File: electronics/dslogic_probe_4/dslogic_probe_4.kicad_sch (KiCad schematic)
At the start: 16 parts, among them J1 Conn_02x04_Odd_Even, J2 Conn_02x04_Odd_Even

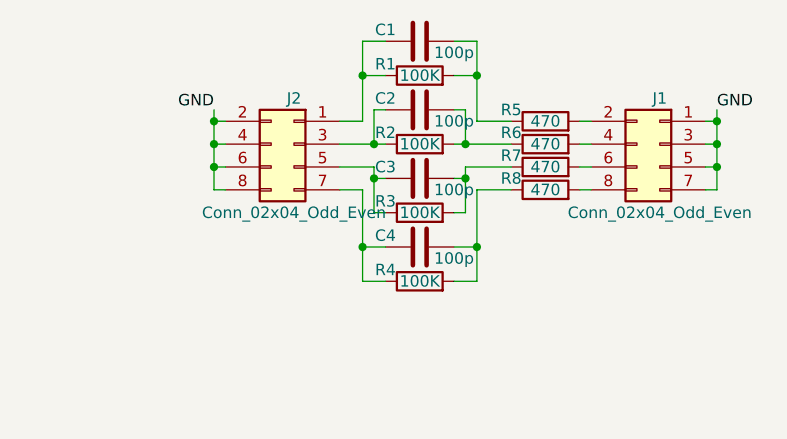
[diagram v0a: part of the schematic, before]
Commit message: edge footprints for probes
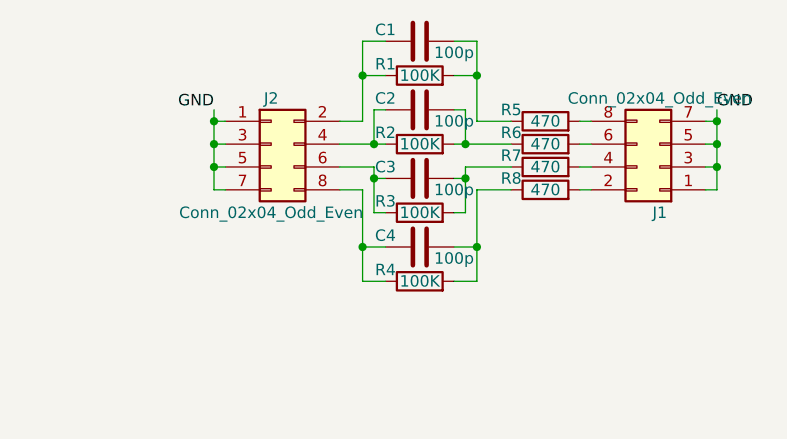
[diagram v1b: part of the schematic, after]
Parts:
- J1, J2: footprint Connector_PinSocket_1.27mm:PinSocket_2x04_P1.27mm_Vertical -> SquantorConnectors:Header-0127-2X04-EDGE
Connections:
- net GND: now also J2.1 (Pin_1), J2.3 (Pin_3), J2.5 (Pin_5), J2.7 (Pin_7); no longer J2.2 (Pin_2), J2.4 (Pin_4), J2.6 (Pin_6), J2.8 (Pin_8)
- net at C3.1, R3.1: now also J2.6 (Pin_6); no longer J2.5 (Pin_5)
- net at C1.1, R1.1: now also J2.2 (Pin_2); no longer J2.1 (Pin_1)
- net at C2.1, R2.1: now also J2.4 (Pin_4); no longer J2.3 (Pin_3)
- net at C4.1, R4.1: now also J2.8 (Pin_8); no longer J2.7 (Pin_7)
- net at R6.2: now also J1.6 (Pin_6); no longer J1.4 (Pin_4)
- net at J1.2 (Pin_2): now also R8.2; no longer R5.2
- net at R7.2: now also J1.4 (Pin_4); no longer J1.6 (Pin_6)
- net at J1.8 (Pin_8): now also R5.2; no longer R8.2
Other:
- moved on the sheet: J1
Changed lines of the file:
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@@
     (pin "2")
   )
-  (symbol (lib_id "Connector_Generic:Conn_02x04_Odd_Even") (at 73.66 38.1 0) (mirror y) (unit 1)
-    (in_bom yes) (on_board yes)
-    (property "Reference" "J2" (id 0) (at 73.66 33.02 0))
-    (property "Value" "Conn_02x04_Odd_Even" (id 1) (at 73.66 45.72 0))
-    (property "Footprint" "Connector_PinSocket_1.27mm:PinSocket_2x04_P1.27mm_Vertical" (id 2) (at 73.66 38.1 0)
-      (effects (font (size 1.27 1.27)) hide)
-    )
-    (property "Datasheet" "~" (id 3) (at 73.66 38.1 0)
+  (symbol (lib_id "Connector_Generic:Conn_02x04_Odd_Even") (at 71.12 38.1 0) (unit 1)
+    (in_bom yes) (on_board yes)
+    (property "Reference" "J2" (id 0) (at 71.12 33.02 0))
+    (property "Value" "Conn_02x04_Odd_Even" (id 1) (at 71.12 45.72 0))
+    (property "Footprint" "SquantorConnectors:Header-0127-2X04-EDGE" (id 2) (at 71.12 38.1 0)
+      (effects (font (size 1.27 1.27)) hide)
+    )
+    (property "Datasheet" "~" (id 3) (at 71.12 38.1 0)
       (effects (font (size 1.27 1.27)) hide)
     )
@@
     (pin "2")
   )
-  (symbol (lib_id "Connector_Generic:Conn_02x04_Odd_Even") (at 114.3 38.1 0) (mirror y) (unit 1)
-    (in_bom yes) (on_board yes)
-    (property "Reference" "J1" (id 0) (at 114.3 33.02 0))
-    (property "Value" "Conn_02x04_Odd_Even" (id 1) (at 114.3 45.72 0))
-    (property "Footprint" "Connector_PinSocket_1.27mm:PinSocket_2x04_P1.27mm_Vertical" (id 2) (at 114.3 38.1 0)
-      (effects (font (size 1.27 1.27)) hide)
-    )
-    (property "Datasheet" "~" (id 3) (at 114.3 38.1 0)
+  (symbol (lib_id "Connector_Generic:Conn_02x04_Odd_Even") (at 114.3 40.64 180) (unit 1)
+    (in_bom yes) (on_board yes)
+    (property "Reference" "J1" (id 0) (at 114.3 45.72 0))
+    (property "Value" "Conn_02x04_Odd_Even" (id 1) (at 114.3 33.02 0))
+    (property "Footprint" "SquantorConnectors:Header-0127-2X04-EDGE" (id 2) (at 114.3 40.64 0)
+      (effects (font (size 1.27 1.27)) hide)
+    )
+    (property "Datasheet" "~" (id 3) (at 114.3 40.64 0)
       (effects (font (size 1.27 1.27)) hide)
     )
@@
     )
     (path "/a72f7593-045b-4cee-9761-530bd4867197"
-      (reference "J1") (unit 1) (value "Conn_02x04_Odd_Even") (footprint "Connector_PinSocket_1.27mm:PinSocket_2x04_P1.27mm_Vertical")
+      (reference "J1") (unit 1) (value "Conn_02x04_Odd_Even") (footprint "SquantorConnectors:Header-0127-2X04-EDGE")
     )
     (path "/247d18a8-48ce-4e7f-9759-0eea4ad80e9a"
-      (reference "J2") (unit 1) (value "Conn_02x04_Odd_Even") (footprint "Connector_PinSocket_1.27mm:PinSocket_2x04_P1.27mm_Vertical")
+      (reference "J2") (unit 1) (value "Conn_02x04_Odd_Even") (footprint "SquantorConnectors:Header-0127-2X04-EDGE")
     )
     (path "/00000000-0000-0000-0000-00005ee12bf3"

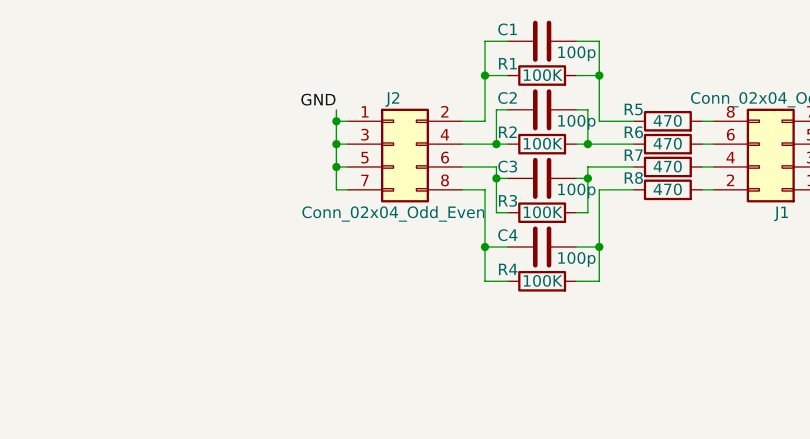
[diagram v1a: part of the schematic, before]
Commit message: updated pinout
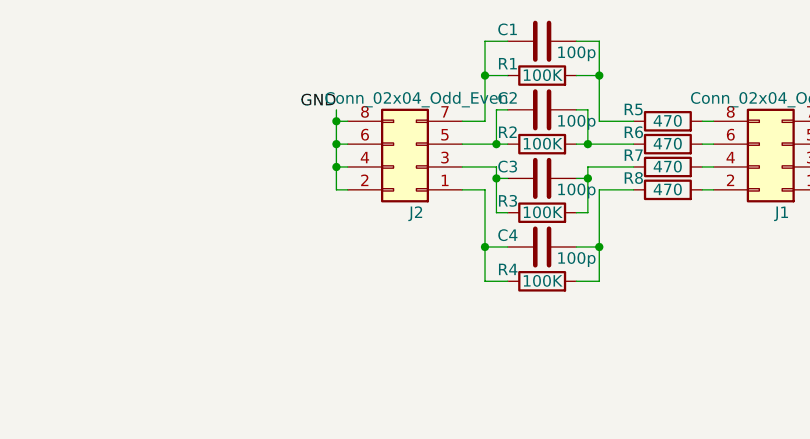
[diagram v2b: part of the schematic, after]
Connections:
- net GND: now also J2.2 (Pin_2), J2.4 (Pin_4), J2.6 (Pin_6), J2.8 (Pin_8); no longer J2.1 (Pin_1), J2.3 (Pin_3), J2.5 (Pin_5), J2.7 (Pin_7)
- net at C3.1, R3.1: now also J2.3 (Pin_3); no longer J2.6 (Pin_6)
- net at C1.1, R1.1: now also J2.7 (Pin_7); no longer J2.2 (Pin_2)
- net at C2.1, R2.1: now also J2.5 (Pin_5); no longer J2.4 (Pin_4)
- net at C4.1, R4.1: now also J2.1 (Pin_1); no longer J2.8 (Pin_8)
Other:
- moved on the sheet: J2
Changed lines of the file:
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@@
     (pin "2")
   )
-  (symbol (lib_id "Connector_Generic:Conn_02x04_Odd_Even") (at 71.12 38.1 0) (unit 1)
+  (symbol (lib_id "Connector_Generic:Conn_02x04_Odd_Even") (at 73.66 40.64 180) (unit 1)
     (in_bom yes) (on_board yes)
-    (property "Reference" "J2" (id 0) (at 71.12 33.02 0))
-    (property "Value" "Conn_02x04_Odd_Even" (id 1) (at 71.12 45.72 0))
-    (property "Footprint" "SquantorConnectors:Header-0127-2X04-EDGE" (id 2) (at 71.12 38.1 0)
+    (property "Reference" "J2" (id 0) (at 73.66 45.72 0))
+    (property "Value" "Conn_02x04_Odd_Even" (id 1) (at 73.66 33.02 0))
+    (property "Footprint" "SquantorConnectors:Header-0127-2X04-EDGE" (id 2) (at 73.66 40.64 0)
       (effects (font (size 1.27 1.27)) hide)
     )
-    (property "Datasheet" "~" (id 3) (at 71.12 38.1 0)
+    (property "Datasheet" "~" (id 3) (at 73.66 40.64 0)
       (effects (font (size 1.27 1.27)) hide)
     )

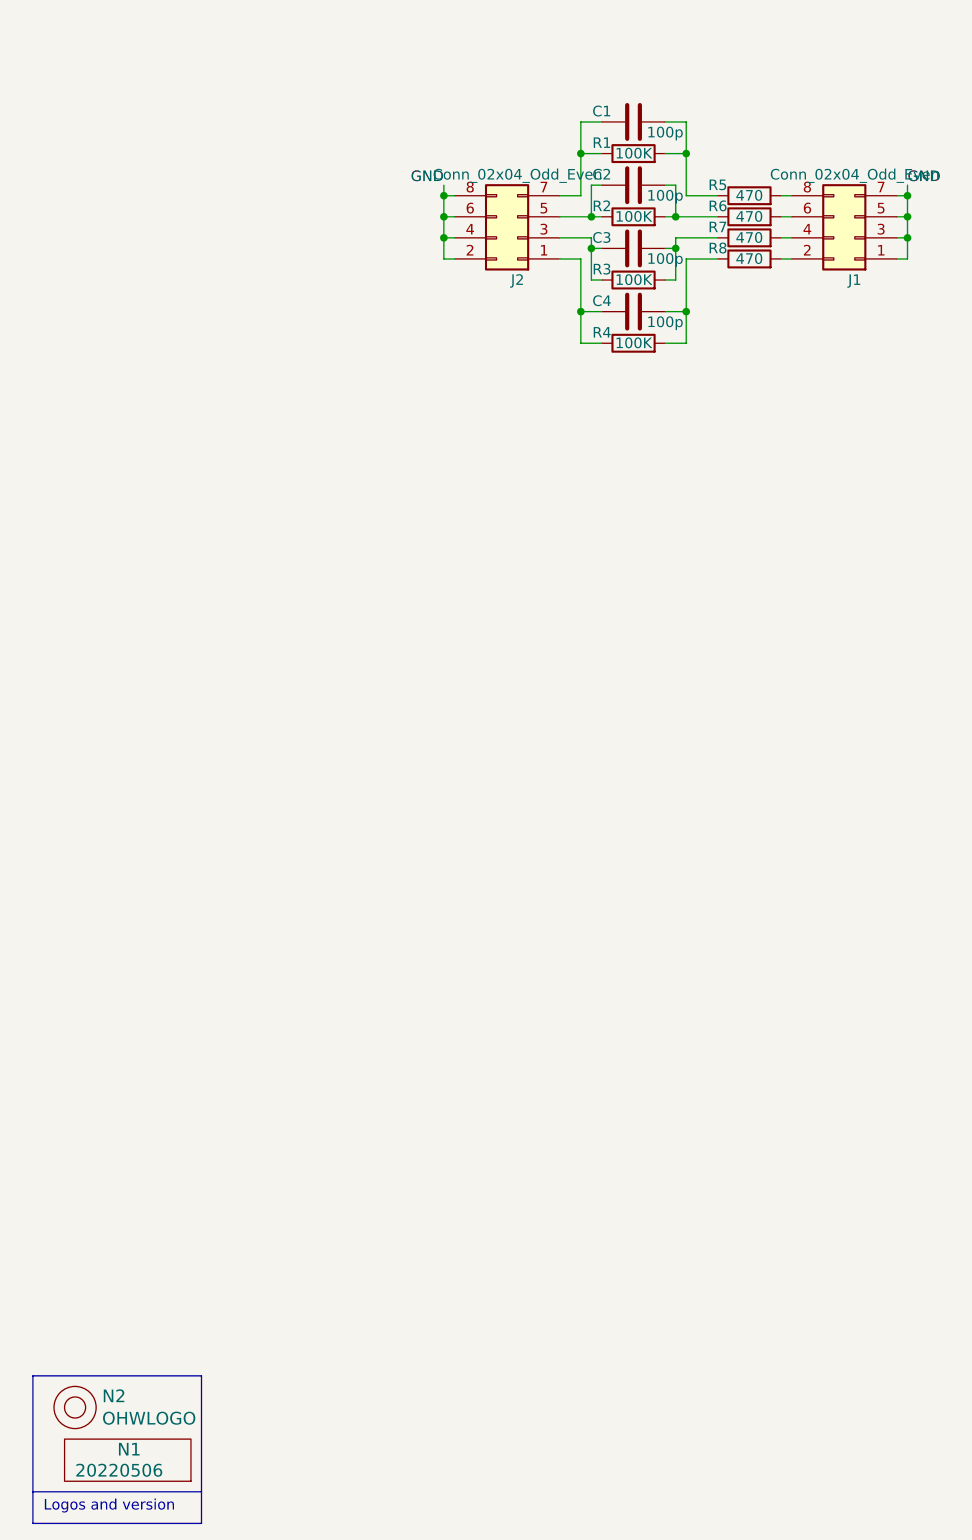
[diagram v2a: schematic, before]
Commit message: reviewd 4 bit logic probe circuit
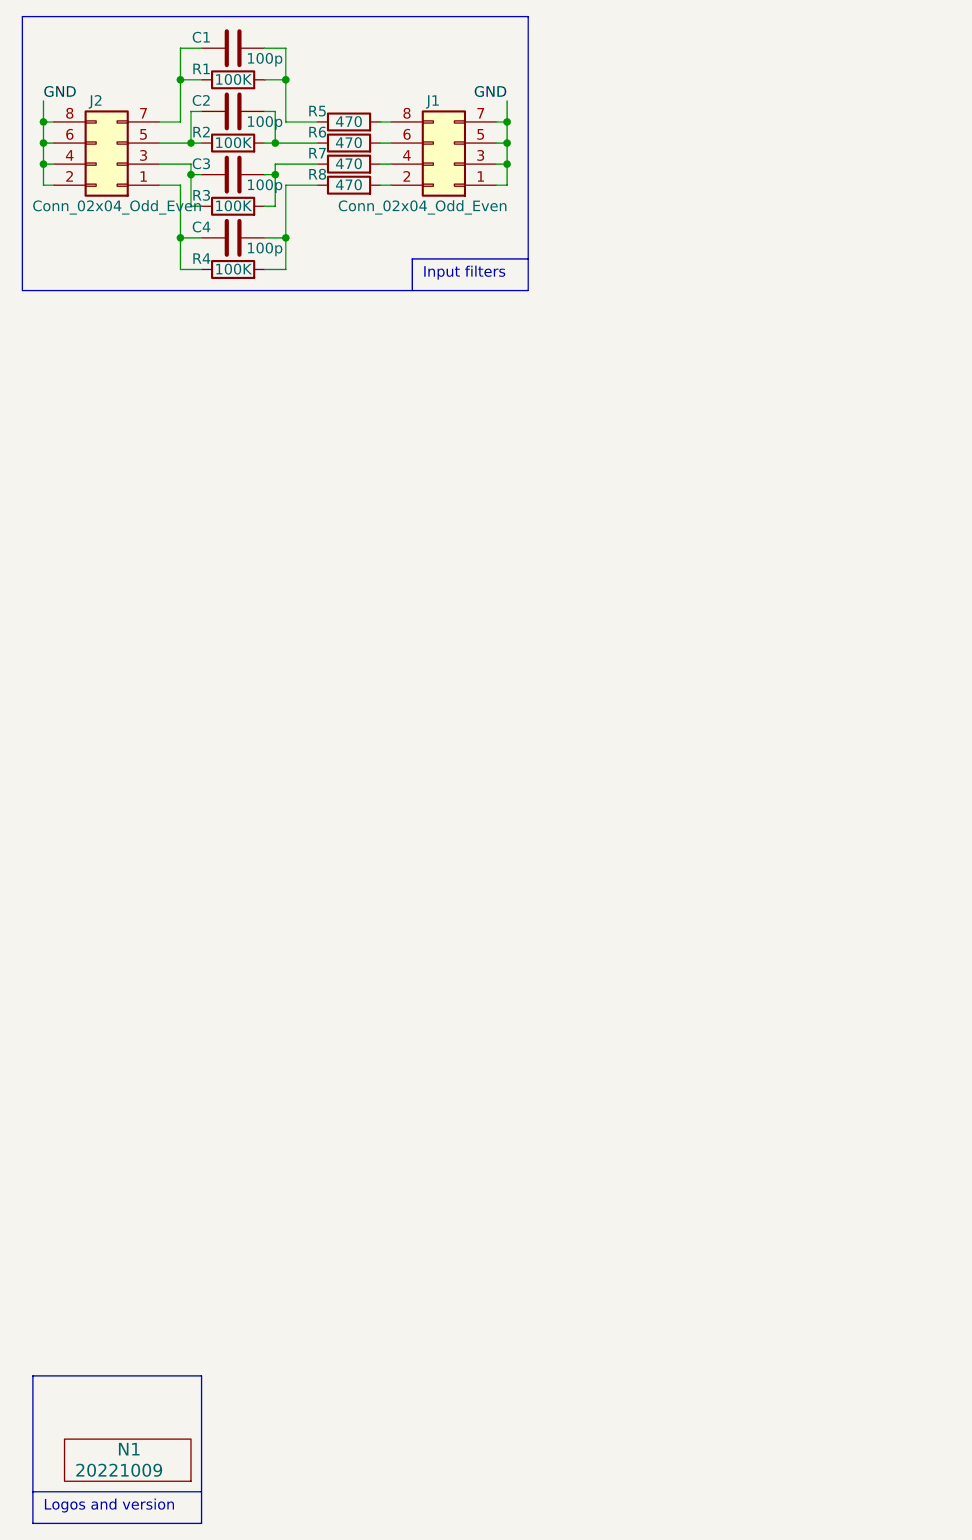
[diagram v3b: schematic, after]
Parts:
- removed N2: OHWLOGO, Symbol:OSHW-Symbol_6.7x6mm_SilkScreen, symbol SquantorLabels:OHWLOGO
- N1: value 20220506 -> 20221009
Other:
- note added: "Input filters"
- moved on the sheet: C1, C2, C3, C4, J1, J2, R1, R2, R3, R4, R5, R6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
